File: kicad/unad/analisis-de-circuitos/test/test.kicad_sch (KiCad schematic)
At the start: 2 parts

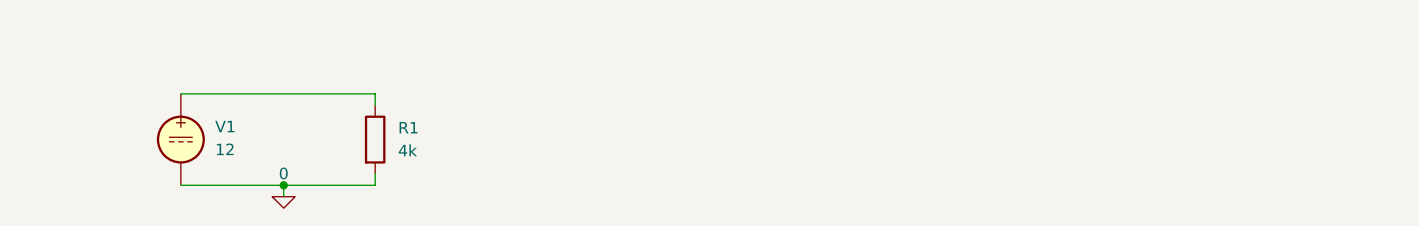
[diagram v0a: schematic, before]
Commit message: kicad/unad/analisis-de-circuitos: Solve problems 62 and 63 from page 38
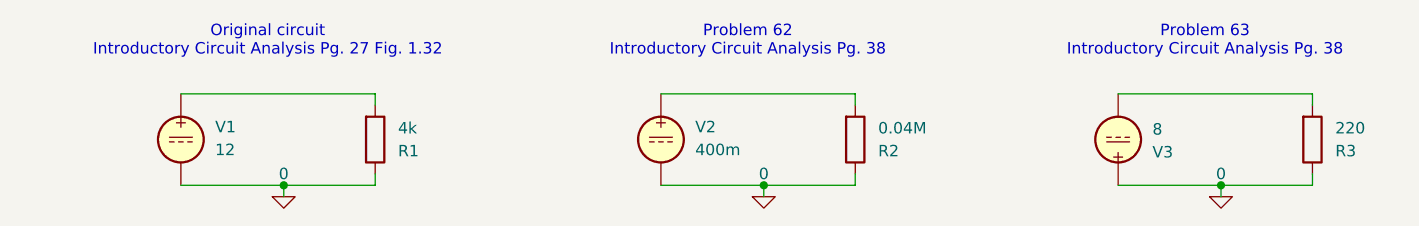
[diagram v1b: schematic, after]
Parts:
- added R2: 0.04M, symbol Device:R
- added R3: 220, symbol Device:R
- added V2: 400m, symbol Simulation_SPICE:VDC
- added V3: 8, symbol Simulation_SPICE:VDC
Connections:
- net 0: now also R1.1, R2.1, R3.1, V2.2, V3.1; no longer R1.2
- net at V1.1: now also R1.2; no longer R1.1
- new net: R2.2, V2.1
- new net: R3.2, V3.2
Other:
- note added: "Original circuit Introductory Circuit Analysis Pg. 27 Fig. 1.32"
- note added: "Problem 62 Introductory Circuit Analysis Pg. 38"
- note added: "Problem 63 Introductory Circuit Analysis Pg. 38"
